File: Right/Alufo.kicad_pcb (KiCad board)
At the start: 2 copper layers, 139.7 x 88.9 mm, 67 parts, among them J2 USB_C_Receptacle_USB2.0_16P_2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, J4 USB_C_Receptacle_USB2.0_16P_2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, K11 PG1350, K12 PG1350, K13 PG1350, K14 PG1350, K15 PG1350, K16 PG1350, K21 PG1350, K22 PG1350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

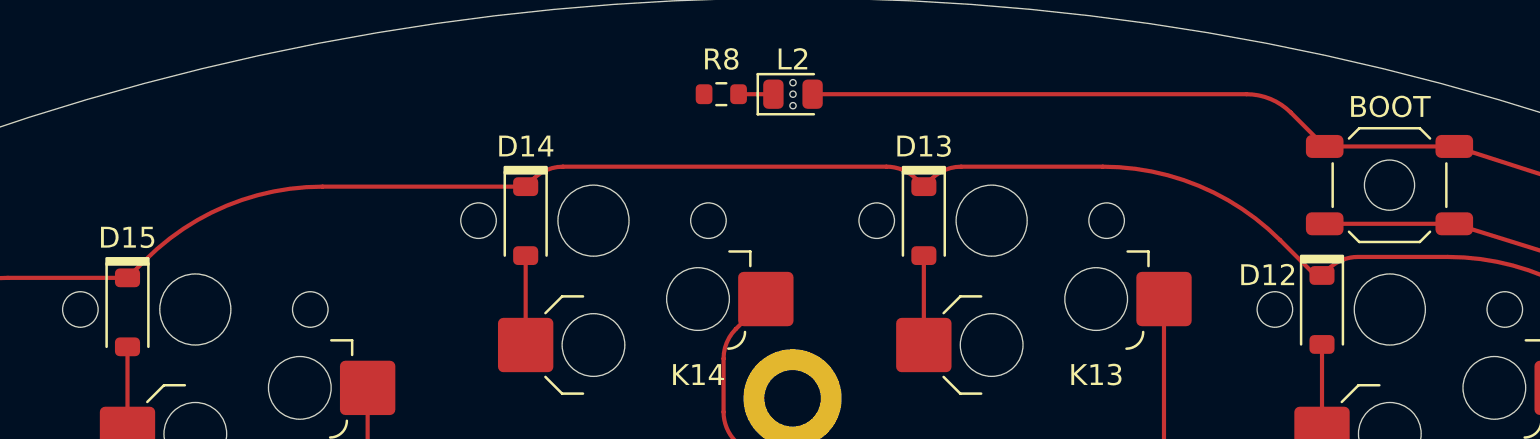
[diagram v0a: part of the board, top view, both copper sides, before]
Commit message: Fix boot access hole location
Because the lefthand side PCB will become the base for the righthand board (and vice versa), and because the boot button is no longer centred, the hole in the base to allow access to the button must be on the opposite side of the centreline to that button. This means the access hole needs to be a separate component and the boot switch footprint no longer needs a central hole.
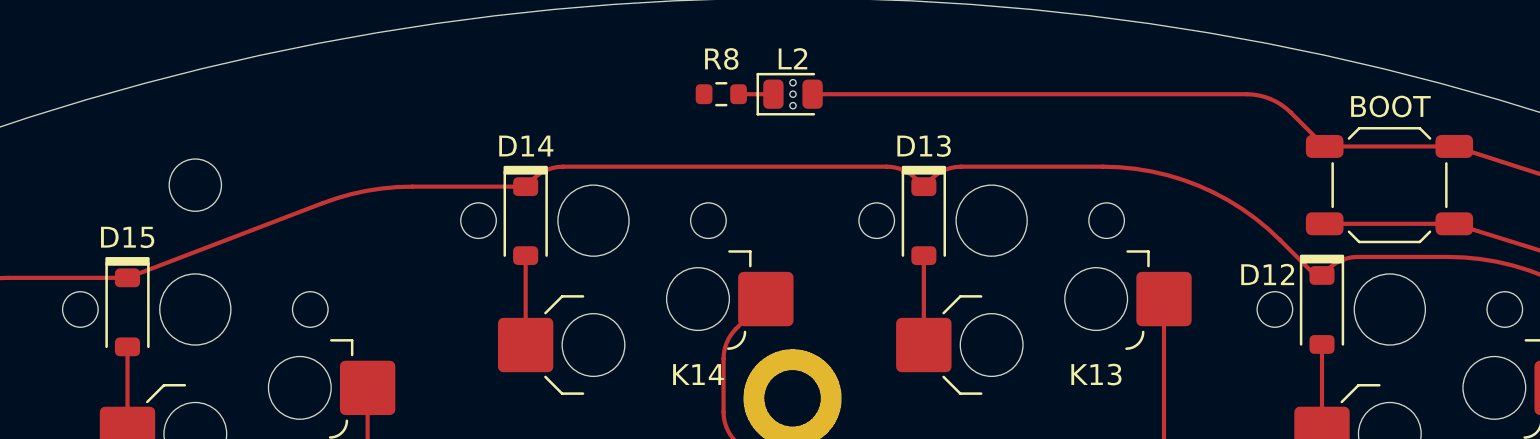
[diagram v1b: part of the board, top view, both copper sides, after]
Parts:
- added H6: BootAccess, MountingHole:MountingHole_2.5mm, F.Cu at (123.8, 38.0)
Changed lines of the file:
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@@
 		)
 	)
+	(footprint "MountingHole:MountingHole_2.5mm"
+		(layer "F.Cu")
+		(at 123.825 37.966677)
+		(descr "Mounting Hole 2.5mm, no annular")
+		(tags "mounting hole 2.5mm no annular")
+		(property "Reference" "H6"
+			(at 0 -3.5 0)
+			(layer "F.SilkS")
+			(hide yes)
+			(effects
+				(font
+					(size 1 1)
+					(thickness 0.15)
+				)
+			)
+		)
+		(property "Value" "BootAccess"
+			(at 0 3.5 0)
+			(layer "F.Fab")
+			(hide yes)
+			(effects
+				(font
+					(size 1 1)
+					(thickness 0.15)
+				)
+			)
+		)
+		(property "Footprint" "MountingHole:MountingHole_2.5mm"
+			(at 0 0 0)
+			(unlocked yes)
+			(layer "F.Fab")
+			(hide yes)
+			(effects
+				(font
+					(size 1.27 1.27)
+					(thickness 0.15)
+				)
+			)
+		)
+		(property "Datasheet" ""
+			(at 0 0 0)
+			(unlocked yes)
+			(layer "F.Fab")
+			(hide yes)
+			(effects
+				(font
+					(size 1.27 1.27)
+					(thickness 0.15)
+				)
+			)
+		)
+		(property "Description" "Mounting Hole without connection"
+			(at 0 0 0)
+			(unlocked yes)
+			(layer "F.Fab")
+			(hide yes)
+			(effects
+				(font
+					(size 1.27 1.27)
+					(thickness 0.15)
+				)
+			)
+		)
+		(property ki_fp_filters "MountingHole*")
+		(sheetname "Root")
+		(sheetfile "Alufo.kicad_sch")
+		(attr exclude_from_pos_files exclude_from_bom)
+		(fp_circle
+			(center 0 0)
+			(end 2.5 0)
+			(stroke
+				(width 0.15)
+				(type solid)
+			)
+			(fill none)
+			(layer "Cmts.User")
+		)
+		(fp_circle
+			(center 0 0)
+			(end 2.75 0)
+			(stroke
+				(width 0.05)
+				(type solid)
+			)
+			(fill none)
+			(layer "F.CrtYd")
+		)
+		(fp_text user "${REFERENCE}"
+			(at 0 0 0)
+			(layer "F.Fab")
+			(effects
+				(font
+					(size 1 1)
+					(thickness 0.15)
+				)
+			)
+		)
+		(pad "" np_thru_hole circle
+			(at 0 0)
+			(size 2.5 2.5)
+			(drill 2.5)
+			(layers "*.Cu" "*.Mask")
+		)
+	)
 	(footprint "Project Library:D_SOD-123_Mod"
 		(layer "F.Cu")
@@
 		)
 		(fp_text user "No F.Cu tracks"
-			(at 2.5 0.2 0)
+			(at -2.5 0.2 0)
 			(layer "Cmts.User")
 			(effects
@@
 			)
 		)
-		(fp_text user "No F.Cu tracks"
-			(at -2.5 0.2 0)
+		(fp_text user "KEEP-OUT ZONE"
+			(at -2.5 -0.2 0)
 			(layer "Cmts.User")
 			(effects
@@
 			)
 		)
-		(fp_text user "KEEP-OUT ZONE"
-			(at -2.5 -0.2 0)
+		(fp_text user "No F.Cu tracks"
+			(at 2.5 0.2 0)
 			(layer "Cmts.User")
 			(effects
@@
 			)
 		)
-		(pad "" np_thru_hole circle
-			(at 0 0 180)
-			(size 2.4 2.4)
-			(drill 2.4)
-			(layers "F.Mask")
-		)
 		(pad "1" smd roundrect
 			(at -3.1 -1.85 180)
@@
 	)
 	(segment
-		(start 120.58 42.402177)
-		(end 121.428283 41.553894)
-		(width 0.2)
-		(layer "F.Cu")
-		(net 2)
-	)
-	(segment
 		(start 207.222719 51.774719)
 		(end 209.682748 54.234748)
@@
 	)
 	(segment
+		(start 134.202833 38.039176)
+		(end 139.63 38.039176)
+		(width 0.2)
+		(layer "F.Cu")
+		(net 2)
+	)
+	(segment
 		(start 160.463603 37.084)
 		(end 167.241437 37.084)
@@
 	)
 	(segment
+		(start 120.58 42.402177)
+		(end 129.915588 38.831164)
+		(width 0.2)
+		(layer "F.Cu")
+		(net 2)
+	)
+	(segment
 		(start 196.436679 49.116679)
 		(end 192.236718 44.916718)
@@
 	)
 	(segment
-		(start 129.913564 38.039176)
-		(end 139.63 38.039176)
-		(width 0.2)
-		(layer "F.Cu")
-		(net 2)
-	)
-	(segment
 		(start 158.310611 37.669787)
 		(end 158.68 38.039176)
@@
 	)
 	(arc
+		(start 134.202833 38.039176)
+		(mid 132.022941 38.238834)
+		(end 129.915588 38.831164)
+		(width 0.2)
+		(layer "F.Cu")
+		(net 2)
+	)
+	(arc
 		(start 156.896397 37.084)
 		(mid 157.661764 37.236241)
@@
 		(width 0.2)
 		(layer "F.Cu")
-		(net 2)
-	)
-	(arc
-		(start 121.428283 41.553894)
-		(mid 125.321363 38.952621)
-		(end 129.913564 38.039176)
-		(width 0.2)
-		(layer "F.Cu")

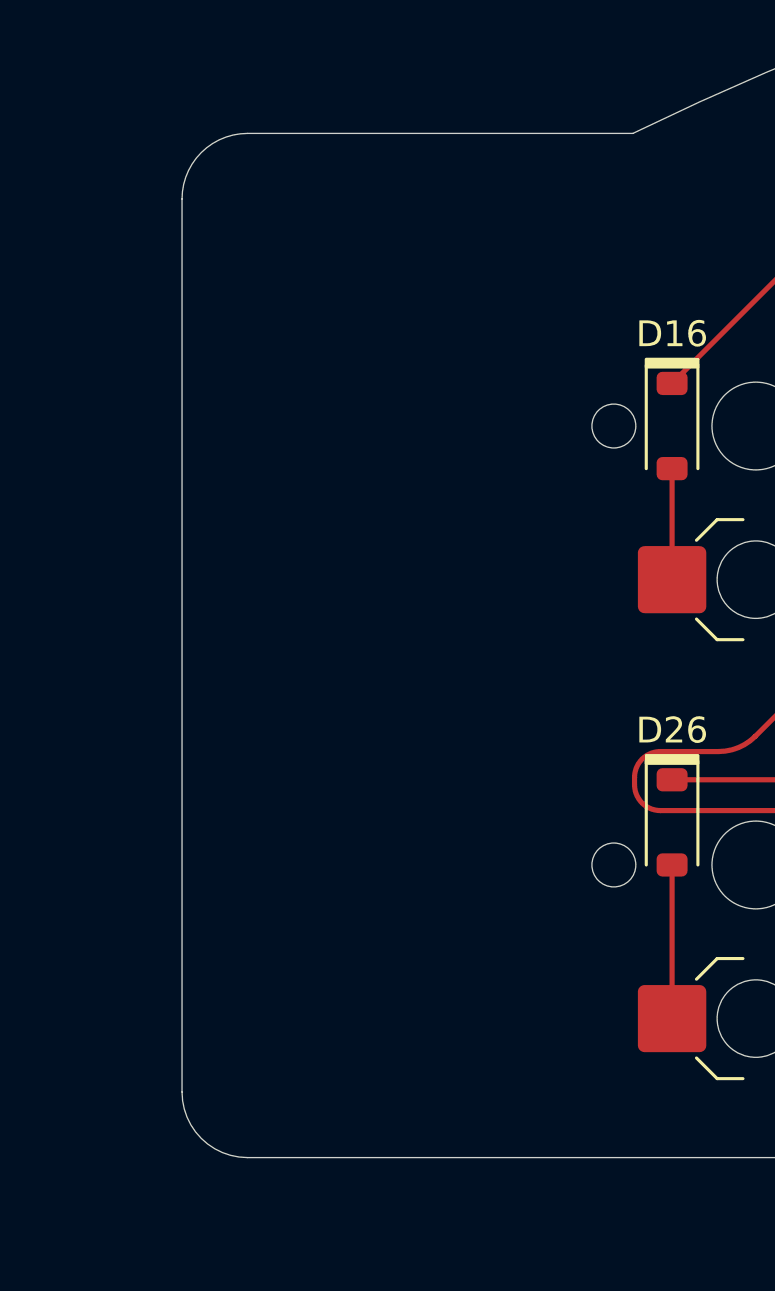
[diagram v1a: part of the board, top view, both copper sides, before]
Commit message: Add “crop circle” image to righthand side, update title block and dynamic text
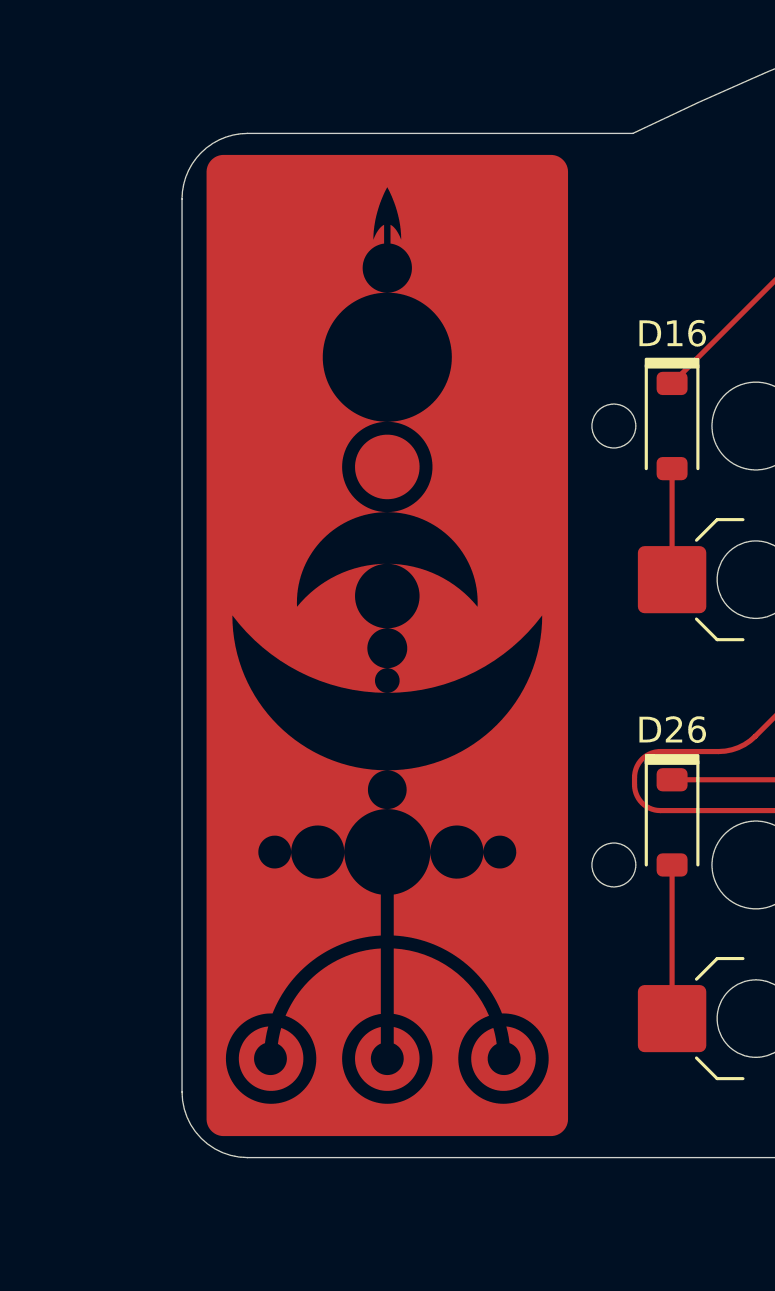
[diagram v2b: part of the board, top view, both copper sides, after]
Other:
- board text added: "${COMPANY}"
- board text added: "${TITLE} v${REVISION}"
- board text removed: "${AUTHOR}"

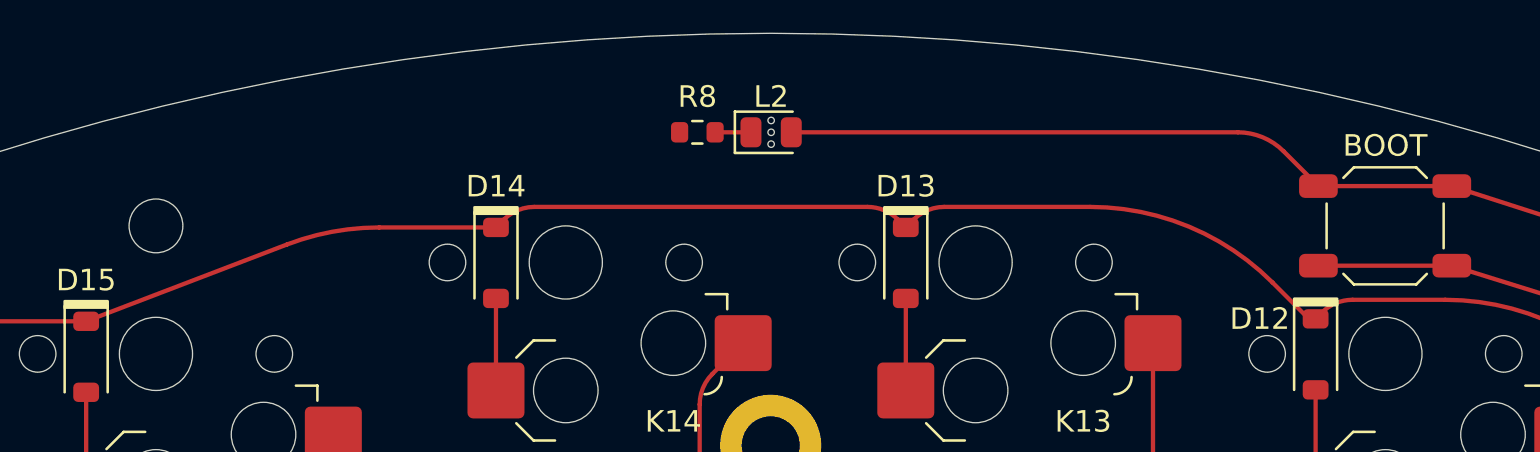
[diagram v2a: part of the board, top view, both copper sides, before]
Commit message: Revert boot access hole change
It was correct before!
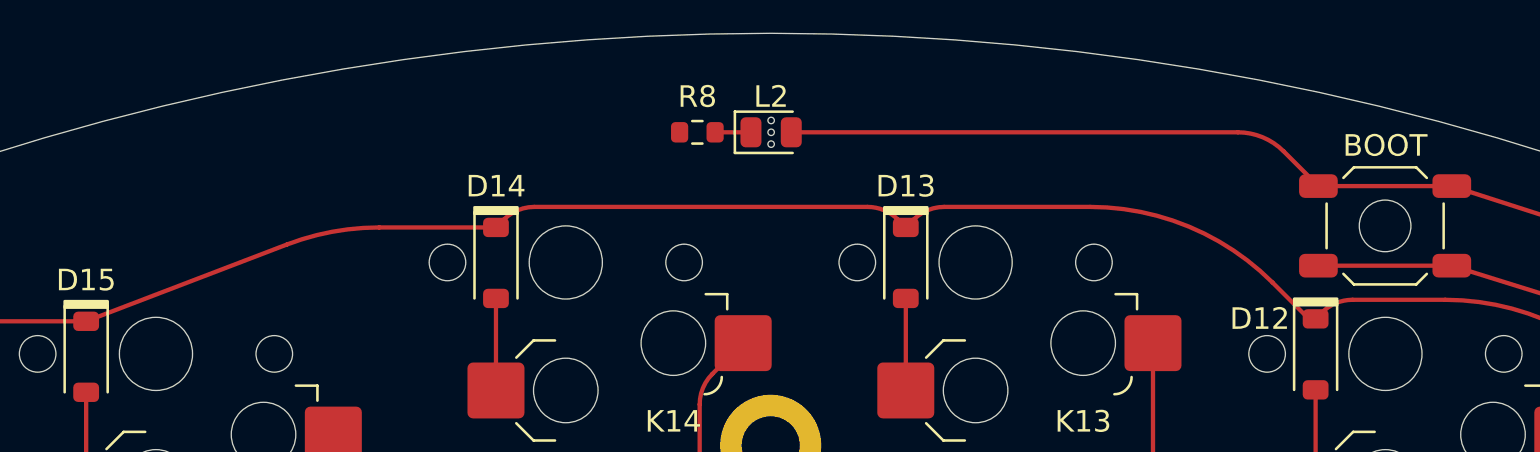
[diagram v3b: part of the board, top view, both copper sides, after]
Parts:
- removed H6: BootAccess, MountingHole:MountingHole_2.5mm
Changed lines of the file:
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@@
 		)
 	)
-	(footprint "MountingHole:MountingHole_2.5mm"
-		(layer "F.Cu")
-		(at 123.825 37.966677)
-		(descr "Mounting Hole 2.5mm, no annular")
-		(tags "mounting hole 2.5mm no annular")
-		(property "Reference" "H6"
-			(at 0 -3.5 0)
-			(layer "F.SilkS")
-			(hide yes)
-			(effects
-				(font
-					(size 1 1)
-					(thickness 0.15)
-				)
-			)
-		)
-		(property "Value" "BootAccess"
-			(at 0 3.5 0)
-			(layer "F.Fab")
-			(hide yes)
-			(effects
-				(font
-					(size 1 1)
-					(thickness 0.15)
-				)
-			)
-		)
-		(property "Footprint" "MountingHole:MountingHole_2.5mm"
-			(at 0 0 0)
-			(unlocked yes)
-			(layer "F.Fab")
-			(hide yes)
-			(effects
-				(font
-					(size 1.27 1.27)
-					(thickness 0.15)
-				)
-			)
-		)
-		(property "Datasheet" ""
-			(at 0 0 0)
-			(unlocked yes)
-			(layer "F.Fab")
-			(hide yes)
-			(effects
-				(font
-					(size 1.27 1.27)
-					(thickness 0.15)
-				)
-			)
-		)
-		(property "Description" "Mounting Hole without connection"
-			(at 0 0 0)
-			(unlocked yes)
-			(layer "F.Fab")
-			(hide yes)
-			(effects
-				(font
-					(size 1.27 1.27)
-					(thickness 0.15)
-				)
-			)
-		)
-		(property ki_fp_filters "MountingHole*")
-		(sheetname "Root")
-		(sheetfile "Alufo.kicad_sch")
-		(attr exclude_from_pos_files exclude_from_bom)
-		(fp_circle
-			(center 0 0)
-			(end 2.5 0)
-			(stroke
-				(width 0.15)
-				(type solid)
-			)
-			(fill none)
-			(layer "Cmts.User")
-		)
-		(fp_circle
-			(center 0 0)
-			(end 2.75 0)
-			(stroke
-				(width 0.05)
-				(type solid)
-			)
-			(fill none)
-			(layer "F.CrtYd")
-		)
-		(fp_text user "${REFERENCE}"
-			(at 0 0 0)
-			(layer "F.Fab")
-			(effects
-				(font
-					(size 1 1)
-					(thickness 0.15)
-				)
-			)
-		)
-		(pad "" np_thru_hole circle
-			(at 0 0)
-			(size 2.5 2.5)
-			(drill 2.5)
-			(layers "*.Cu" "*.Mask")
-		)
-	)
 	(footprint "Project Library:D_SOD-123_Mod"
 		(layer "F.Cu")
@@
 		)
 		(fp_text user "KEEP-OUT ZONE"
-			(at -2.5 -0.2 0)
+			(at 2.5 -0.2 0)
 			(layer "Cmts.User")
 			(effects
@@
 		)
 		(fp_text user "KEEP-OUT ZONE"
-			(at 2.5 -0.2 0)
+			(at -2.5 -0.2 0)
 			(layer "Cmts.User")
 			(effects
@@
 			)
 		)
+		(pad "" np_thru_hole circle
+			(at 0 0 180)
+			(size 2.4 2.4)
+			(drill 2.4)
+			(layers "F.Mask")
+		)
 		(pad "1" smd roundrect

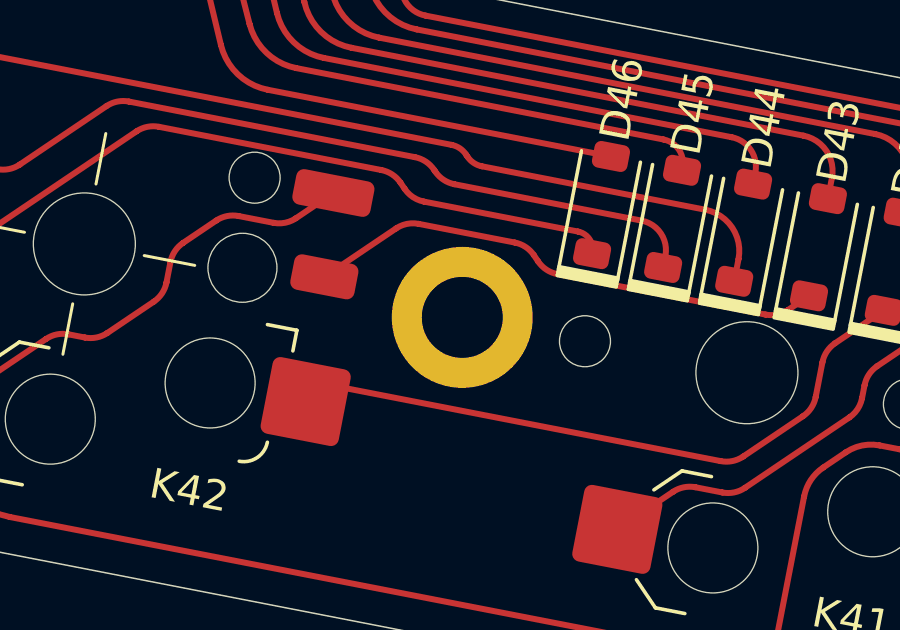
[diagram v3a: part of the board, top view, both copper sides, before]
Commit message: Fix alignment of thumb cluster screw hole
It did not line up when one side’s PCB was used as a base for the other.
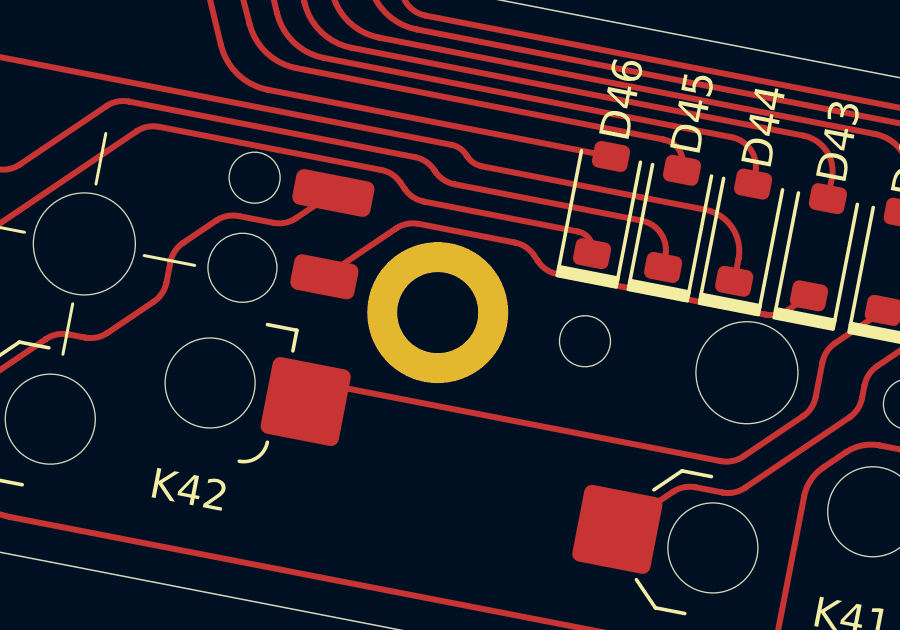
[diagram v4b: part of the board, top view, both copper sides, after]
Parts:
- moved H5 0.83 mm to (185.0, 102.8)
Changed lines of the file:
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@@
 	(footprint "Project Library:MountingHole_2.2mm_M2_SMD_Solder_Nut"
 		(layer "F.Cu")
-		(at 185.773435 102.988868)
+		(at 184.955415 102.829864)
 		(descr "Mounting Hole 2.2mm, M2, DIN965")
 		(tags "mounting hole 2.2mm m2 din965")
@@
 		(layer "Cmts.User")
 	)
+	(gr_line
+		(start 195.2625 104.833358)
+		(end 184.955415 102.829864)
+		(stroke
+			(width 0.2)
+			(type default)
+		)
+		(layer "Cmts.User")
+	)
